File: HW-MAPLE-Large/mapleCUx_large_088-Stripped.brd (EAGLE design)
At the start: 100 x 59 mm, 56 parts, among them IC1 DS2482, IC2 LAN-USR-ES1, Q1 BSS84, X4 1751248, X7 1751264

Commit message: Cleanup + Stripped Version
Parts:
- removed CTX-DB: 1365-10, con-leotronics:1365-10
- removed ESP8266: ESP03, esp8266modules:ESP03
- removed IC1: DS2482, 1wire:SO08
- removed Q1: BSS84, transistor-small-signal:SOT23
- removed R1: 4k7, rcl:R0805
- removed R2: 4K7, rcl:R0805
- removed R4: 100, rcl:R0805
- removed RX, TX: (no value), jumper:SJ
- removed X6: (no value), adafruit:U.FL
- removed ZD1: DS9503P, 1wire:TSOC6
- moved C9 15.5 mm to (90.4, 16.8)
- moved R5 14.9 mm to (82.4, 12.3), turned to 180 degrees
- moved R3 14.6 mm to (87.2, 12.4)
- moved RS485 14.5 mm to (84.3, 17.2)
- moved 3V3 7.85 mm to (77.5, 19.6)
- moved 5V 7.85 mm to (77.5, 15.7)
- moved GND 7.41 mm to (77.5, 11.4)
- moved C11 2.30 mm to (63.1, 52.3)
- moved F1 1.93 mm to (89.2, 8.89), turned to 180 degrees
- moved C12 1.37 mm to (59.1, 30.6), turned to 180 degrees
- moved X1 0.80 mm to (99.9, 12.2)
- moved C8 0.63 mm to (64.1, 38.8), turned to 0 degrees
- moved C4 0.57 mm to (72.1, 55.4)
- moved C3 0.51 mm to (27.9, 41.0)
- moved C1 0.51 mm to (28.4, 3.25)
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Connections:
- removed net N$12: ESP8266.ANT, X6.3
- removed net N$18: ESP8266.URXD, RX.2
- removed net N$19: ESP8266.UTXD, TX.2
- removed net N$47: IC1.6, Q1.1
- removed net N$48: IC1.2, Q1.3, ZD1.6
- removed net N$52: Q1.2, R4.1
- removed net N$8: CTX-DB.7
- removed net NC: CTX-DB.9
- net 1W: no longer ZD1.1
- net CC_CS2: no longer IC1.5, R1.2
- net CC_IN_2: no longer IC1.4, R2.2
- net GD: no longer ZD1.2
- net GND: no longer CTX-DB.3, CTX-DB.5, ESP8266.GND, ESP8266.GPIO15, IC1.3, IC1.7, IC1.8, X6.1, X6.2, ZD1.5
- net N$11: no longer ESP8266.GPIO0
- net N$17: no longer ESP8266.CH_PD
- net NRESET: no longer CTX-DB.10
- net RX_DBG: no longer TX.1
- net SWCLK/TCK: no longer CTX-DB.4
- net SWDIO/TMS: no longer CTX-DB.2
- net SWO/TDO: no longer CTX-DB.6
- net TDI: no longer CTX-DB.8
- net TX_DBG: no longer RX.1
- net VCC: no longer CTX-DB.1, ESP8266.VCC
- net VDD: no longer IC1.1, R1.1, R2.1, R4.2
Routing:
- net CC_IN_2: track 120.3 -> 33.6 mm, vias 3 -> 0
- net GND: track 607.5 -> 523.9 mm, vias 3 -> 2
- net CC_CS2: track 117.9 -> 36.7 mm, vias 2 -> 1
- net VCC: track 328.9 -> 291.0 mm, vias 0 -> 1
- net N$11: track 74.6 -> 46.4 mm
- net CE-A: track 53.7 -> 77.4 mm, vias 2 -> 0
- net MISO1: track 155.8 -> 179.3 mm
- net N$21: track 31.6 -> 54.5 mm
- net N$17: track 59.6 -> 37.2 mm
- net SWDIO/TMS: track 21.0 -> 0.00 mm
- net SCK1: track 171.5 -> 152.1 mm, vias 3 -> 2
- net SWCLK/TCK: track 17.6 -> 0.00 mm
- net SWO/TDO: track 15.6 -> 0.00 mm
- net TX_DBG: track 68.0 -> 52.8 mm, vias 1 -> 0
- net RX_DBG: track 73.2 -> 58.4 mm, vias 1 -> 2
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- added copper zone on layer 1, net GND
- added copper zone on layer 16, net GND
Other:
- board text added: "MAPLE CUN - large (stripped)"
- board text added: "MAPLE CUN Stripped 1.4"
- board text added: "V1.4 www.neuby.de"
- board text removed: "ESP-03"
- board text removed: "ESP->MAPLE"
- board text removed: "MAPLE CUN - large (A)"
- board text removed: "MAPLE CUN Lage Version A 1.3"
- board text removed: "V1.3 www.neuby.de"

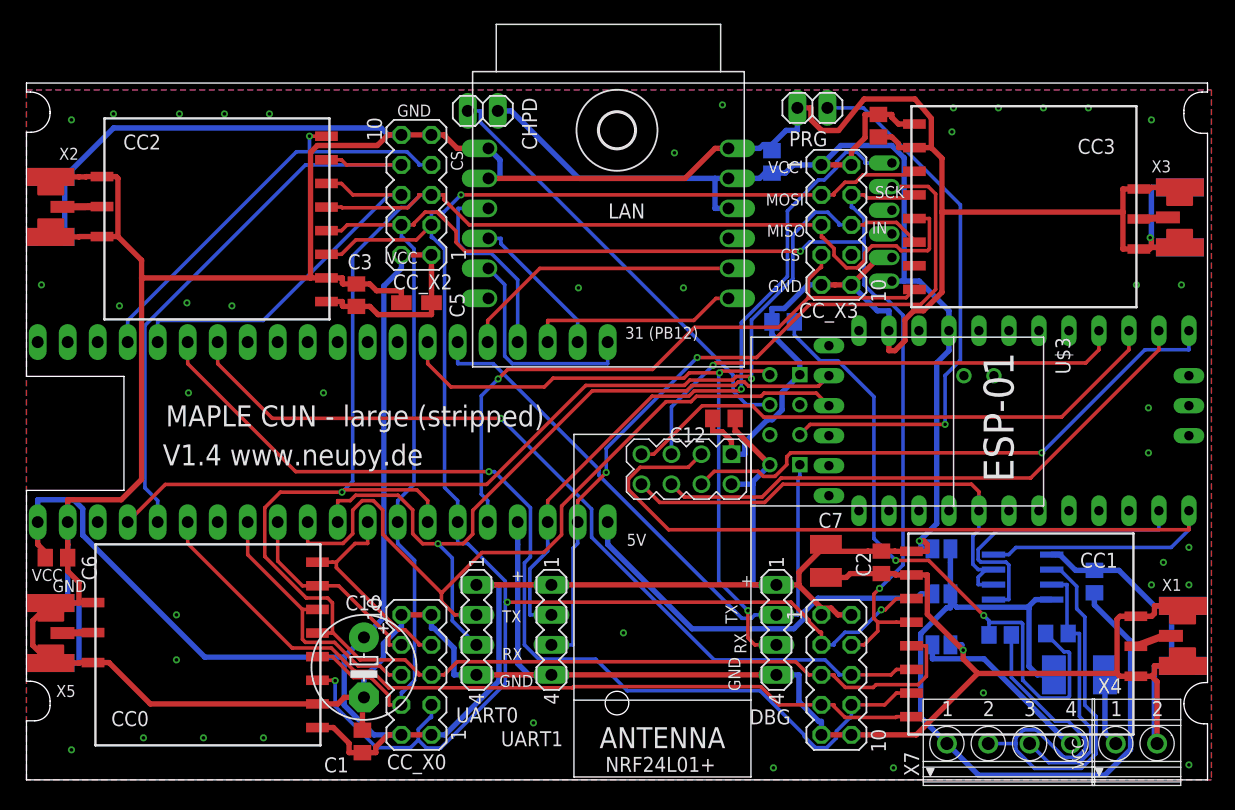
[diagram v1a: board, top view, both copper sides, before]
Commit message: Small Fixes + other RX+TX Pins at Arduino
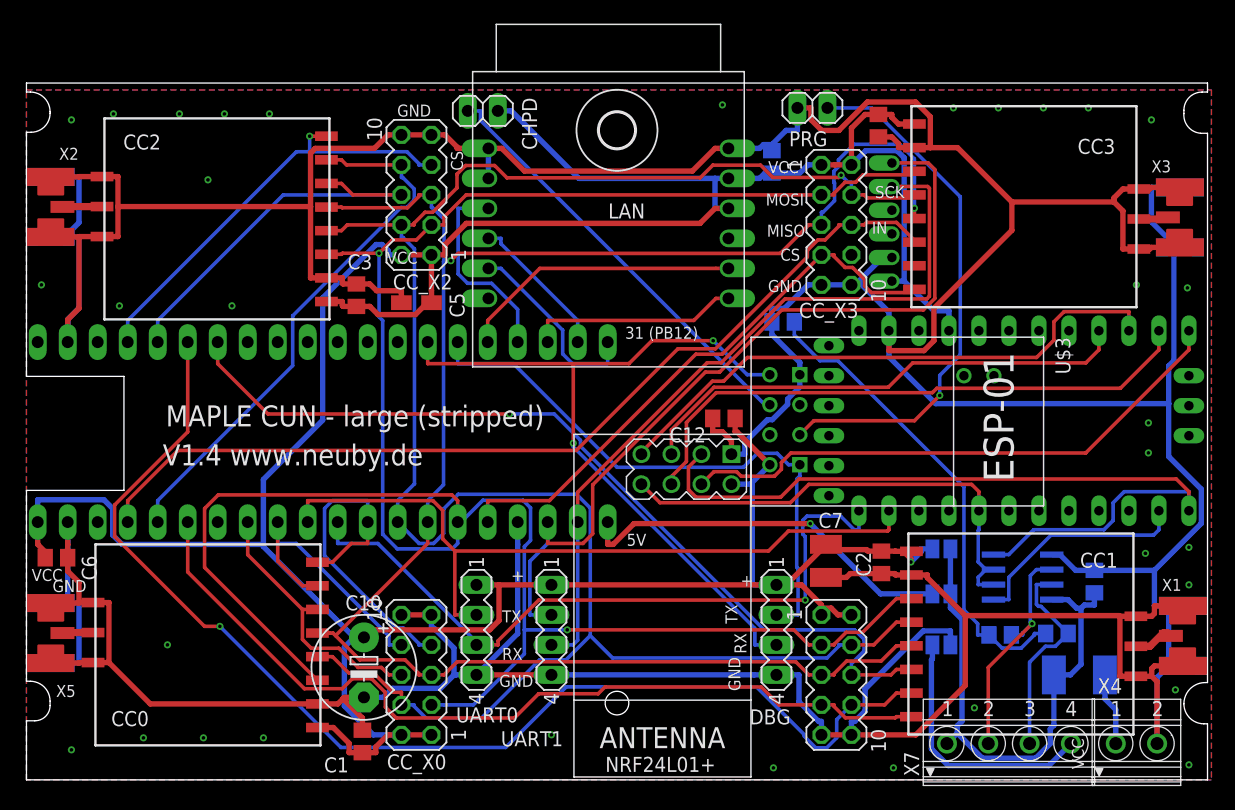
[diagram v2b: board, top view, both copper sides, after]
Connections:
- net GND: now also U$1.2
- net RX-MAPLE: now also U$2.TX0; no longer U$2.TX0-1
- net TX-MAPLE: now also U$2.RX1; no longer U$2.RX1-1
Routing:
- net MOSI1: track 159.5 -> 192.9 mm, vias 4 -> 2
- net GND: track 523.9 -> 556.5 mm, vias 2 -> 0
- net 1W: track 49.2 -> 20.1 mm, vias 0 -> 1
- net MISO1: track 179.3 -> 156.9 mm, vias 1 -> 2
- net VDD: track 67.3 -> 45.1 mm
- net SCK1: track 152.1 -> 171.4 mm, vias 2 -> 1
- net CC_OUT_1: track 87.0 -> 101.1 mm
- net N$21: track 54.5 -> 40.6 mm, vias 2 -> 0
- net CC_CS0: track 18.0 -> 28.7 mm
- net TX1: track 60.9 -> 70.7 mm, vias 1 -> 0
- net CE-A: track 77.4 -> 70.0 mm
- net CC_CS3: track 55.5 -> 48.4 mm, vias 1 -> 0
- net CC_OUT_0: track 17.2 -> 23.8 mm
- net RX_DBG: track 58.4 -> 64.8 mm
- net RO-A: track 25.5 -> 19.2 mm
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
